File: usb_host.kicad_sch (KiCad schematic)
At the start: 9 parts, among them J2 10.0QCHTZ6.8, Q2 2N7002, Q3 AO3401A, U6 H5VU25UC

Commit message: Rev.2 (260322)
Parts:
- added Q4: AO3401A, Package_TO_SOT_SMD:SOT-23, symbol Transistor_FET:AO3401A
- C22: LCSC (none) -> C16780
- D4: renamed from D3; LCSC (none) -> C20615804
- J2: LCSC (none) -> C404967
- Q2: LCSC (none) -> C8545
- Q3: LCSC (none) -> C15127
- R16: renamed from R15; LCSC (none) -> C25741
- R17: renamed from R16; LCSC (none) -> C25092
- R18: renamed from R17; LCSC (none) -> C25092
- U6: symbol Hakodate_Board:H5VU25UC -> Harucom_Board:H5VU25UC; LCSC (none) -> C20615800
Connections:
- net VBUS: now also Q4.2 (S); no longer Q3.3 (D)
- net at Q2.3 (D), Q3.1 (G), R16.2: now also Q4.1 (G)
- new net: Q3.3 (D), Q4.3 (D)
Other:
- moved on the sheet: Q2, Q3, R16

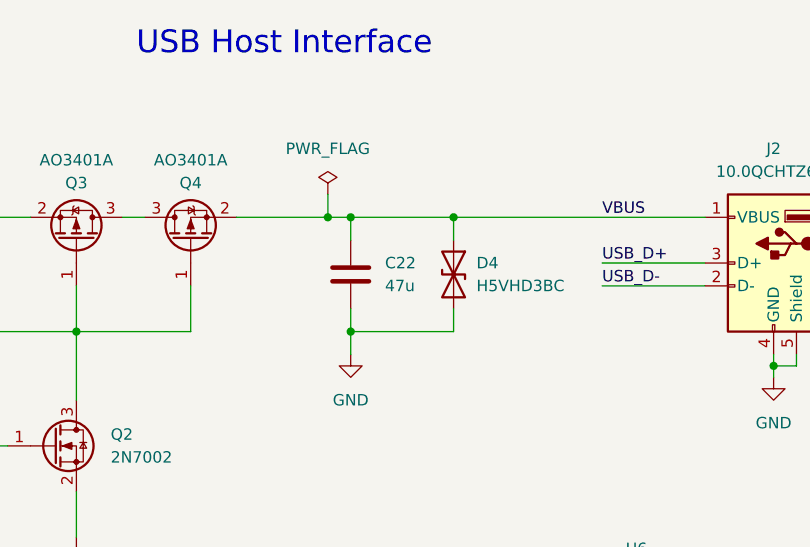
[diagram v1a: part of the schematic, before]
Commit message: Rev. 2B: Change PSRAM package from SOP-8 to USON-8L.
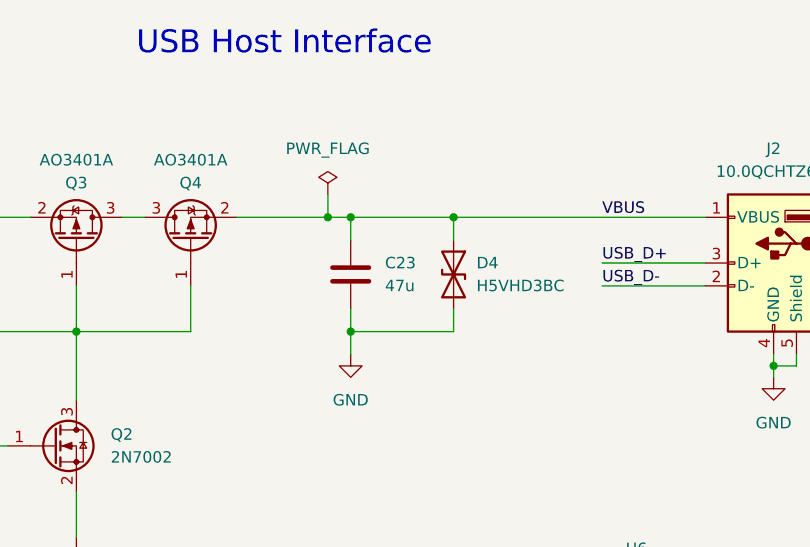
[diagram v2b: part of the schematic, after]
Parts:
- renumbered C22 to C23
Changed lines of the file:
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@@
 	(title_block
 		(title "Harucom-board")
-		(date "2026-03-22")
-		(rev "2")
+		(date "2026-03-23")
+		(rev "2B")
 		(comment 1 "https://github.com/harukasan/harucom-board/")
 		(comment 2 "SPDX-License-Identifier: CERN-OHL-P-2.0")
@@
 		(dnp no)
 		(fields_autoplaced yes)
-		(property "Reference" "C22"
+		(property "Reference" "C23"
 			(at 157.48 76.1999 0)
 			(effects
@@
 			(project "hakodate-board"
 				(path "/0cb5192e-ac62-478f-bacb-beb1b9be1a5b/02ac8dfd-aa97-4c6d-8242-cde94b0dfa94"
-					(reference "C22")
+					(reference "C23")
 					(unit 1)
 				)
